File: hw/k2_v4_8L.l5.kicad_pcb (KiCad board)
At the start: 8 copper layers, 120 x 46 mm, 59 parts, among them J11 J_EC_HEADER, J12 J_12V_IN, J13 J_SWD, J2 SlimSAS_x8_SFF8654, J3 MCIO_4i_SFF1016, J4 MCIO_4i_SFF1016, J6 J_PWR_CTRL, J9 J_OOB_HEADER, U1 STM32G0B1CBT6, U2 DCDC_12V_3V3, U4 BAT54C, U5 OPTO_LTV356T, U6 DS320PR1601

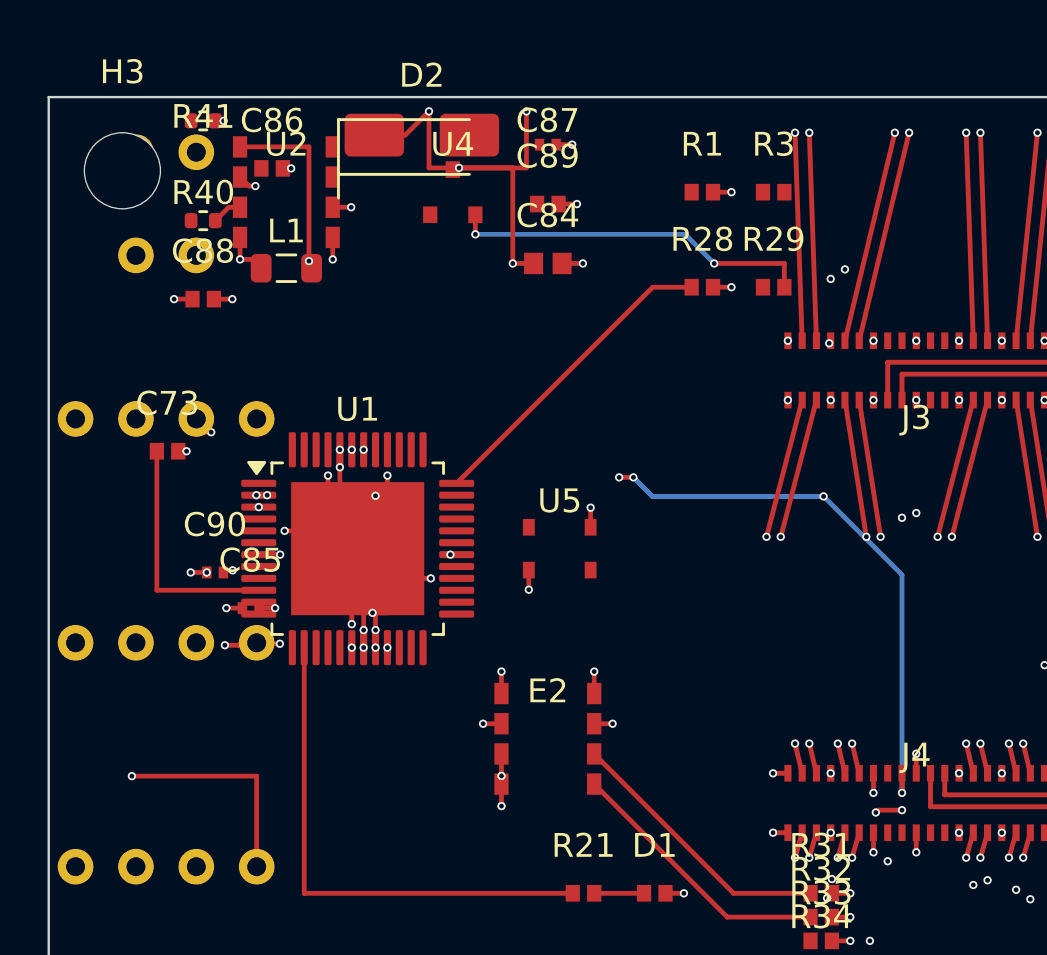
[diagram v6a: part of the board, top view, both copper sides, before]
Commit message: p4(k2): 收敛增量 5（L2 自裁）—— 低速/电源 F.Cu 通道搜索（阶段 F2，精确复核放行）
- 阶段 F2（新器 tools/k2_p4_ls_route_v1.py）：对两端铜岛皆在 F.Cu 且距离 <=20mm 的未连接边，
  做同层 0/45/90° 通道搜索（0.05mm 网格八方向 A*，L 形收尾保证段角合法）；线宽 0.200。
- 放行闸 = 精确复核（逐段与全部异网 F.Cu 铜 / 全部孔(孔-铜 0.25) / 板边 0.3 / 禁 track 禁布区比对），
  栅格仅作剪枝。过程记录：首版无精确复核时曾落 16 条但违规 75->208（shorting 48/clearance 26/mask 67/
  crossing 14/hole 12），根因=多边形焊盘内部漏标+未含孔-铜+格心量化；改为栅格剪枝+精确放行后回归合规。
- 实测：未连接 49 -> 46（+3：P3V3_AUX 1.235 / PERSTA# 6.705 / SWCLK_BOOT0 13.762）；违规 75 -> 75
  （类型集不变、无新增）；判定器 PASS5/FAIL5 集合未变；复跑两次逐字节同 77658bed7efaf508。
- 结论：33 条 <=20mm 边中仅 3 条存在合法 F.Cu 通路 => F.Cu 同层域近耗尽；剩余 46 条出路在跨层
  （B.Cu 近乎空层：39 走线/0 铜区；西侧 J6/J9/J11/J12/J13 为 PTH 可达）+ IC 侧落孔，已登记
  needs-cross-layer-router 16 / no-legal-path-in-fcu 30。
- 边界：未动 l4/设计源板/真源 yaml/criteria/SPEC rev-19..32 原件；未派 WORKER；临时仅 /tmp/opencode。
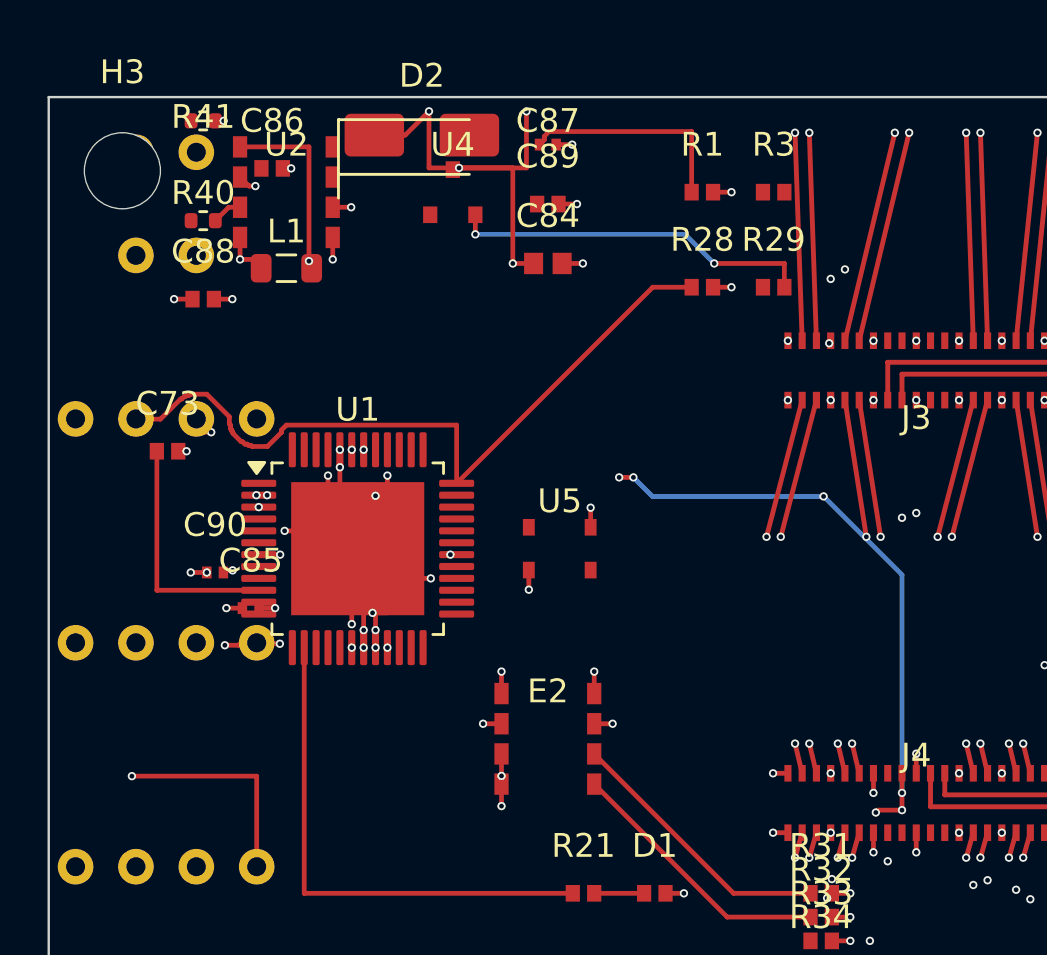
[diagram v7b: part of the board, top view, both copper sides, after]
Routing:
- net SWCLK_BOOT0: track 13.3 -> 31.4 mm
- net PERSTA#: track 0.00 -> 9.27 mm
- net P3V3_AUX: track 35.2 -> 35.9 mm

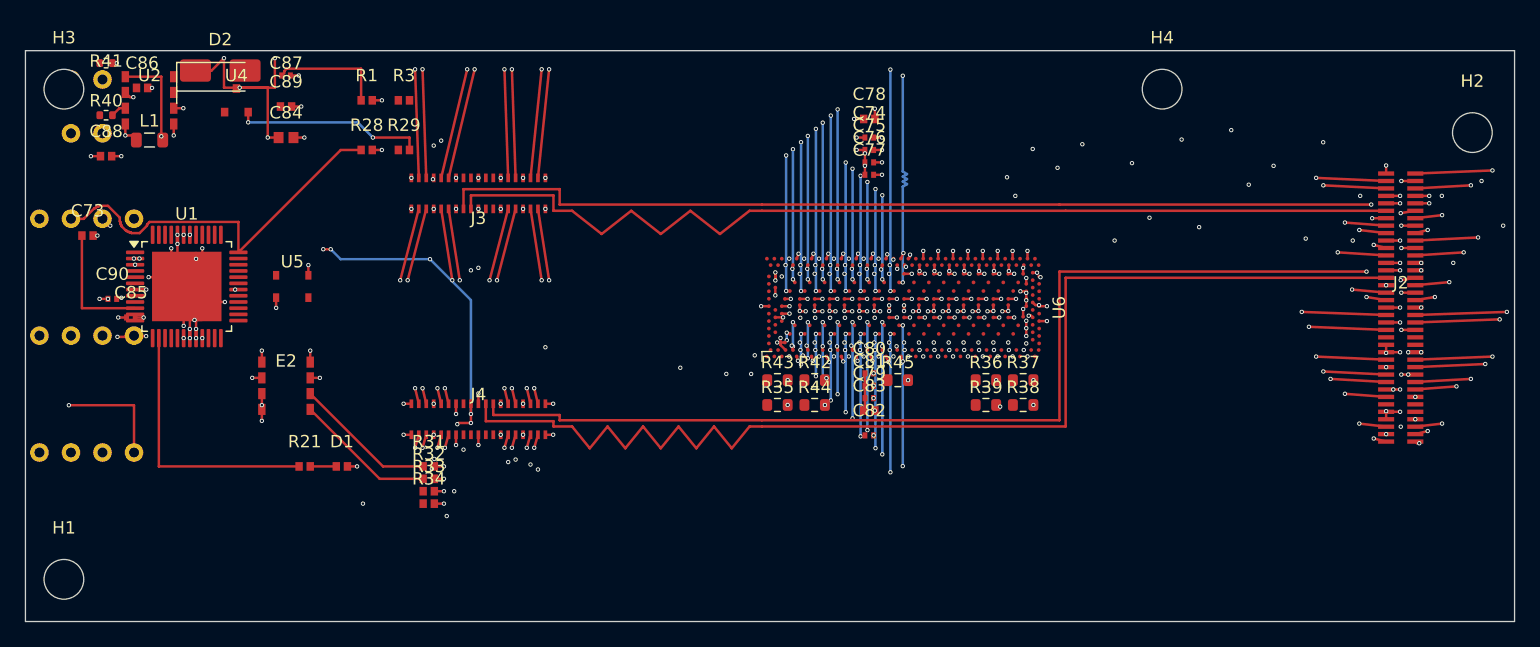
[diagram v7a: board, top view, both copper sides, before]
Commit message: p4(k2): 收敛增量 6（L2 自裁）—— 低速/电源跨层通道布线（阶段 F3）
- 阶段 F3（新器 tools/k2_p4_ls_xlayer_v1.py）：IC 侧落 F->B 通孔（0.20/0.35，板内既有唯一合法孔类）
  + F.Cu 0/45/90 短引线 -> B.Cu 近空层 0/45/90 通道搜索（0.10mm 栅格八方向 A*，L 形收尾）-> 对端
  （既有 B.Cu 铜 / 插件件 PTH 焊盘 / 对端落孔）；线宽 0.200。
- 放行闸 = 精确复核（T-6）：过孔（全铜层净距 + 孔-铜 0.25 + 孔-孔 0.25 无同网豁免 + 板边 0.3 + 禁 via 区）、
  F.Cu 短引线、B.Cu 走线逐项精确比对；栅格仅剪枝。直连分支强制角度判定（首跑曾产生 3 条非 45 段，已修）。
- 实测：未连接 46 -> 31（+15 条，21 支新孔）；违规 75 -> 75（类型集不变、无新增）；判定器 PASS5/FAIL5 集合未变；
  非 45 度 2051 未增；复跑两次逐字节同 87cb6a51c62a61f8。
- 未解登记：no-legal-path-on-bcu 13 / no-legal-via-slot 18（不静默放弃）。
- 边界：未动 l4/设计源板/真源 yaml/criteria/SPEC rev-19..33 原件；未派 WORKER；临时仅 /tmp/opencode。
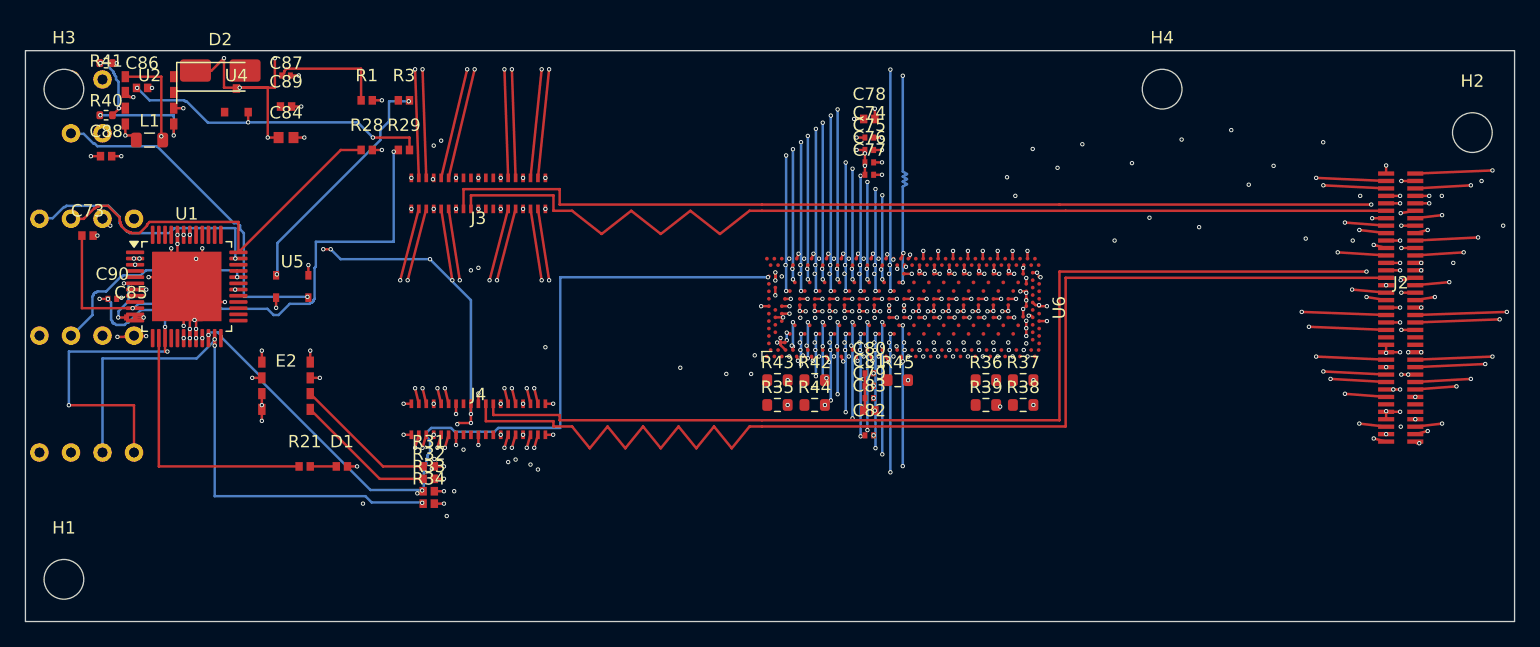
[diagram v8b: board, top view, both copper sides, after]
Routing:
- net I2C2_SCL: track 0.00 -> 69.6 mm, vias 0 -> 4
- net I2C2_SDA: track 0.00 -> 47.2 mm, vias 0 -> 3
- net NRST: track 10.1 -> 44.8 mm, vias 0 -> 2
- net PWR_CTRL_OUT: track 0.00 -> 27.8 mm, vias 0 -> 1
- net P3V3_AUX: track 35.9 -> 58.7 mm, vias 10 -> 12
- net SWDIO: track 0.00 -> 20.4 mm, vias 0 -> 1
- net PWR_BTN_ISO: track 0.00 -> 19.5 mm, vias 0 -> 2
- net UART_RX: track 0.00 -> 17.1 mm, vias 0 -> 1
- net MCU_VDD: track 22.2 -> 36.8 mm, vias 16 -> 18
- net P3V3: track 41.1 -> 48.7 mm, vias 40 -> 41
- net FB_U2: track 1.27 -> 6.02 mm, vias 0 -> 2
